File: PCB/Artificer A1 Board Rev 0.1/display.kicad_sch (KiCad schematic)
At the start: 24 parts

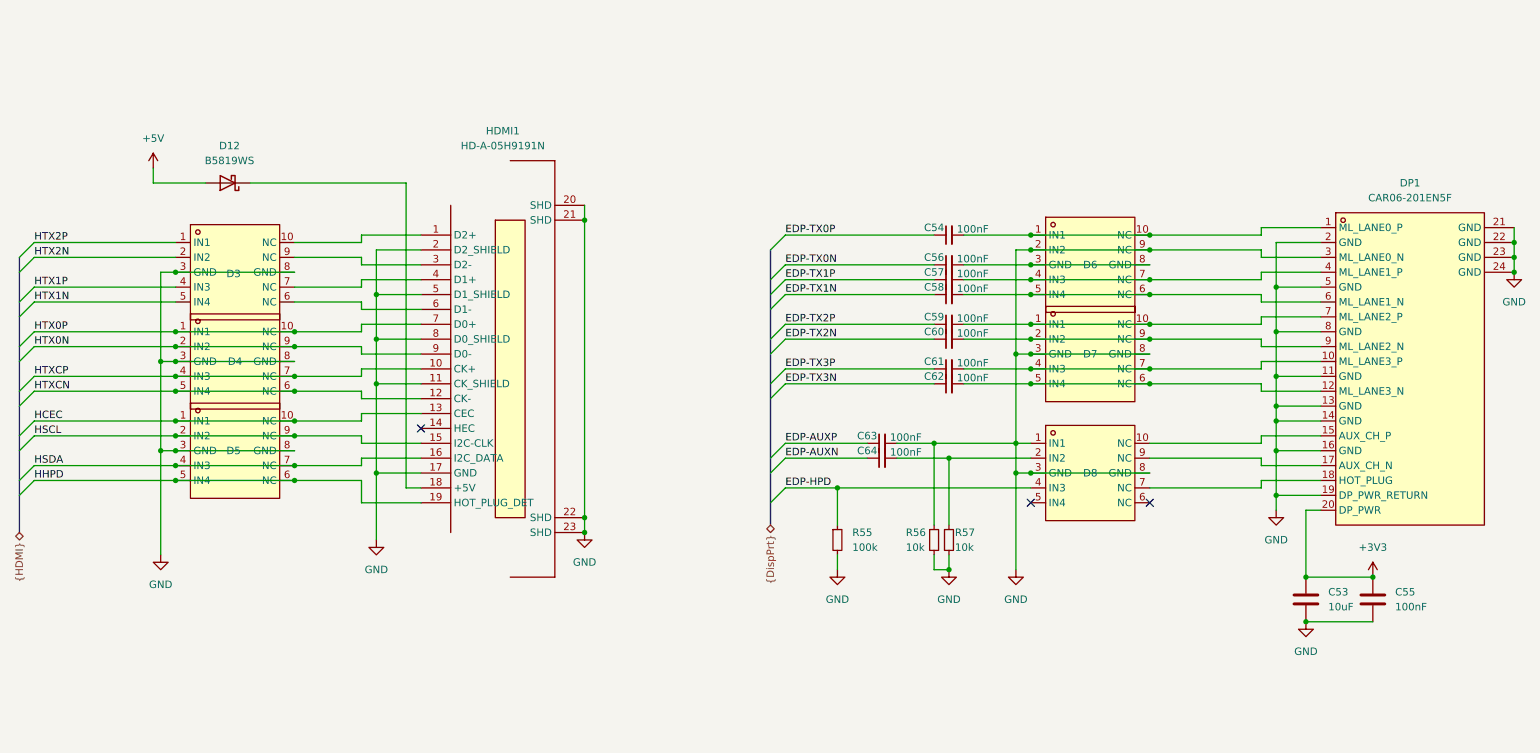
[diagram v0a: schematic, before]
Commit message: cleaned up, kicad 10 & usb c pd
migrated to Kicad 10,
added USB PD for power input
added capacitors inductors and resistor footprints
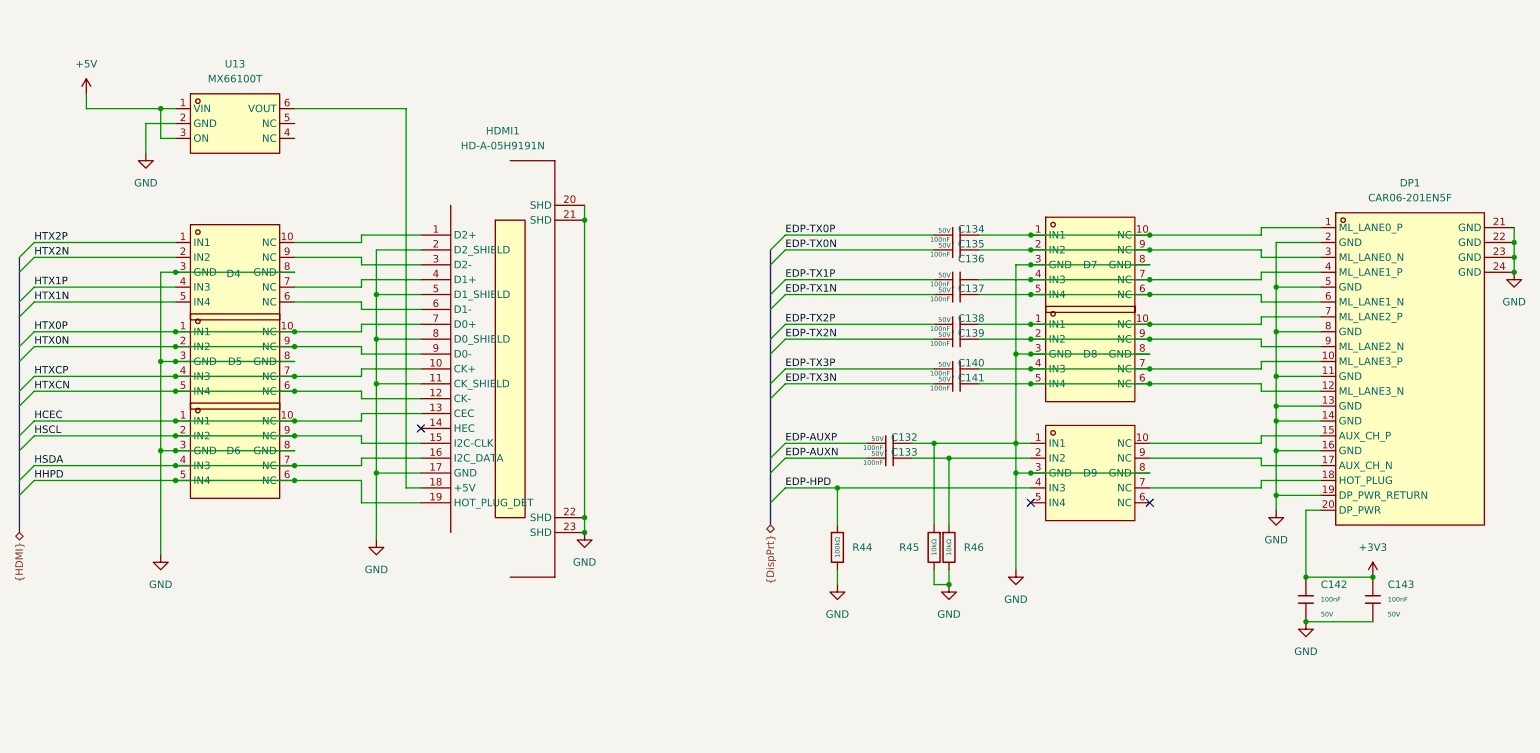
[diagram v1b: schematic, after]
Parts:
- removed C53: 10uF, symbol Device:C
- removed C54, C56, C57, C58, C59, C60, C61, C62, C63, C64: 100nF, symbol Device:C_Small
- removed C55: 100nF, symbol Device:C
- removed D12: B5819WS, Diode_SMD:D_SOD-323_HandSoldering, symbol Device:D_Schottky
- removed R55: 100k, symbol Device:R_Small
- removed R56, R57: 10k, symbol Device:R_Small
- added C132, C133, C134, C135, C136, C137, C138, C139, C140, C141, C142, C143: 100nF, PCM_JLCPCB:C_0402, symbol PCM_JLCPCB-Capacitors:0402,100nF,(2)
- added R44: 100kΩ, PCM_JLCPCB:R_0402, symbol PCM_JLCPCB-Resistors:0402,100kΩ
- added R45, R46: 10kΩ, PCM_JLCPCB:R_0402, symbol PCM_JLCPCB-Resistors:0402,10kΩ
- added U13: MX66100T, easyeda:SOT-23-6_L2.9-W1.6-P0.95-LS2.9-BL, symbol easyeda:MX66100T
- renumbered D3 to D4, D4 to D5, D5 to D6, D6 to D7, D7 to D8, D8 to D9
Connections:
- net +3V3: now also C142.1, C143.1
- net +5V: now also U13.1 (VIN), U13.3 (ON)
- net EDP-AUXN: now also C133.1
- net EDP-AUXP: now also C132.1
- net EDP-HPD: now also R44.1
- net EDP-TX0N: now also C135.1
- net EDP-TX0P: now also C134.1
- net EDP-TX1N: now also C137.1
- net EDP-TX1P: now also C136.1
- net EDP-TX2N: now also C139.1
- net EDP-TX2P: now also C138.1
- net EDP-TX3N: now also C141.1
- net EDP-TX3P: now also C140.1
- net GND: now also D7.3 (GND), D7.8 (GND), C132.2, C142.2, C143.2, R44.2, R45.1, R45.2, R46.2, U13.2 (GND); no longer D7.2 (IN2), D7.9 (NC), DP1.3 (ML_LANE0_N)
- net at D8.1 (IN1), D8.10 (NC), DP1.7 (ML_LANE2_P): now also C138.2
- net at D8.2 (IN2), D8.9 (NC), DP1.9 (ML_LANE2_N): now also C139.2
- net at D8.4 (IN3), D8.7 (NC), DP1.10 (ML_LANE3_P): now also C140.2
- net at D8.5 (IN4), D8.6 (NC), DP1.12 (ML_LANE3_N): now also C141.2
- net at D7.5 (IN4), D7.6 (NC), DP1.6 (ML_LANE1_N): now also C137.2
- net at D9.2 (IN2): now also C133.2, R46.1
- net at D7.4 (IN3), D7.7 (NC), DP1.4 (ML_LANE1_P): now also C136.2
- net at HDMI1.18 (+5V): now also U13.6 (VOUT)
- net at D7.1 (IN1), D7.10 (NC), DP1.1 (ML_LANE0_P): now also C134.2
- new net: C135.2, D7.2 (IN2), D7.9 (NC), DP1.3 (ML_LANE0_N)

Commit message: placed all components
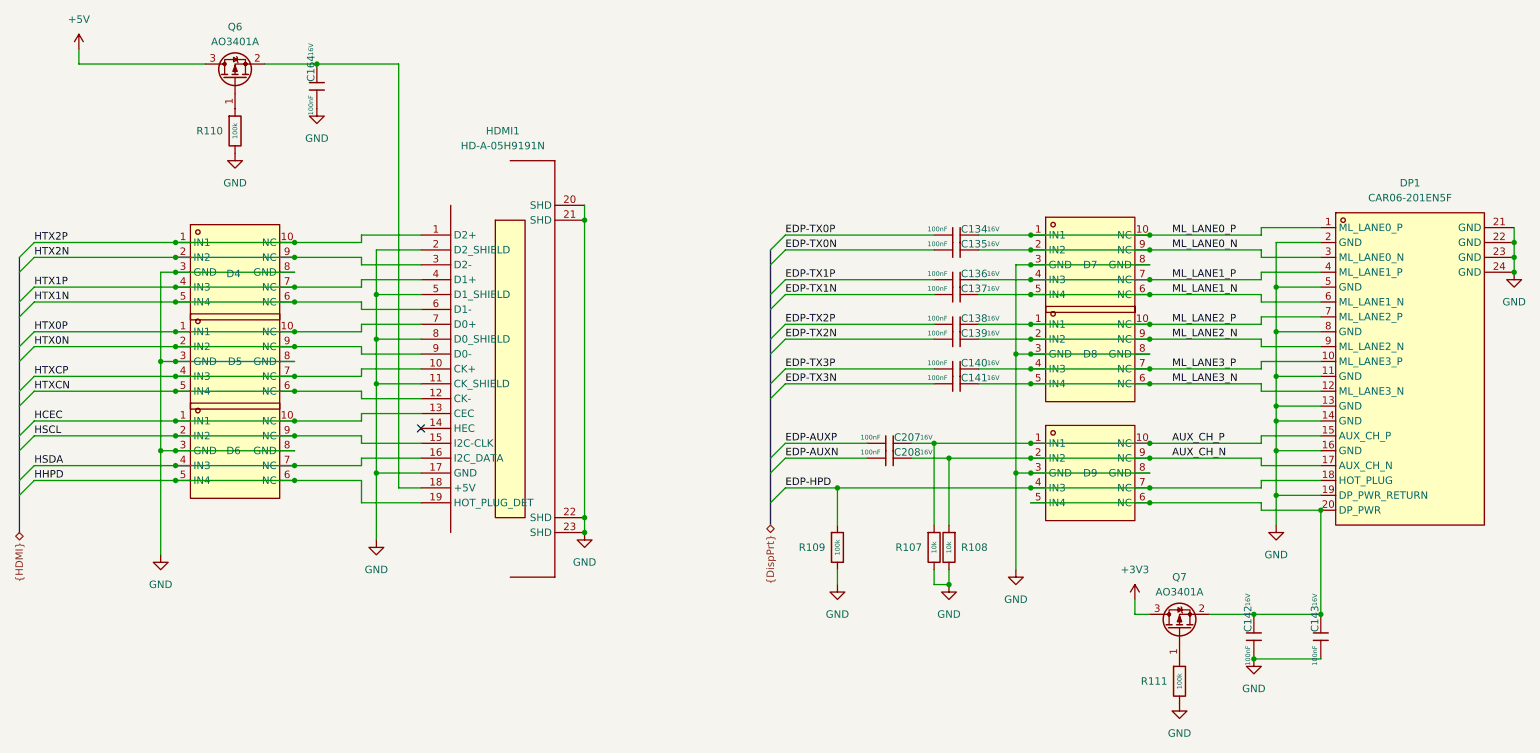
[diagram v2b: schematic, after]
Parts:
- removed C132, C133, C134, C135, C136, C137, C138, C139, C140, C141, C142, C143: 100nF, PCM_JLCPCB:C_0402, symbol PCM_JLCPCB-Capacitors:0402,100nF,(2)
- removed R44: 100kΩ, PCM_JLCPCB:R_0402, symbol PCM_JLCPCB-Resistors:0402,100kΩ
- removed R45, R46: 10kΩ, PCM_JLCPCB:R_0402, symbol PCM_JLCPCB-Resistors:0402,10kΩ
- removed U13: MX66100T, easyeda:SOT-23-6_L2.9-W1.6-P0.95-LS2.9-BL, symbol easyeda:MX66100T
- added C134, C135, C136, C137, C138, C139, C140, C141, C142, C143, C164, C207, C208: 100nF, Capacitor_SMD:C_0201_0603Metric, symbol Cap:JLCPCB_Lib_Blank_Cap
- added Q6, Q7: AO3401A, Package_TO_SOT_SMD:SOT-23, symbol Transistor_FET:AO3401A
- added R107, R108: 10k, Resistor_SMD:R_0201_0603Metric, symbol Cap:JLCPCB_Res_Custom
- added R109, R110, R111: 100k, Resistor_SMD:R_0201_0603Metric, symbol Cap:JLCPCB_Res_Custom
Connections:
- net +3V3: now also Q7.3 (D); no longer DP1.20 (DP_PWR)
- net +5V: now also Q6.3 (D)
- net EDP-AUXN: now also C208.1
- net EDP-AUXP: now also C207.1
- net EDP-HPD: now also D9.7 (NC), DP1.18 (HOT_PLUG), R109.1
- net EDP-TX0N: now also C135.1
- net EDP-TX0P: now also C134.1
- net EDP-TX1N: now also C137.1
- net EDP-TX1P: now also C136.1
- net EDP-TX2N: now also C139.1
- net EDP-TX2P: now also C138.1
- net EDP-TX3N: now also C141.1
- net EDP-TX3P: now also C140.1
- net GND: now also C142.1, C143.1, C164.1, R107.2, R108.2, R109.2, R110.2, R111.2; no longer D9.1 (IN1)
- net HTX1N: now also D4.6 (NC), HDMI1.6 (D1-)
- net HTX1P: now also D4.7 (NC), HDMI1.4 (D1+)
- net HTX2N: now also D4.9 (NC), HDMI1.3 (D2-)
- net HTX2P: now also D4.10 (NC), HDMI1.1 (D2+)
- net AUX_CH_N: now reaches D9.2 (IN2)
- net AUX_CH_N: now also D9.9 (NC), DP1.17 (AUX_CH_N), C208.2, R108.1
- net ML_LANE2_P: now reaches D8.1 (IN1), D8.10 (NC), DP1.7 (ML_LANE2_P)
- net ML_LANE2_P: now also C138.2
- net ML_LANE2_N: now reaches D8.2 (IN2), D8.9 (NC), DP1.9 (ML_LANE2_N)
- net ML_LANE2_N: now also C139.2
- net ML_LANE3_P: now reaches D8.4 (IN3), D8.7 (NC), DP1.10 (ML_LANE3_P)
- net ML_LANE3_P: now also C140.2
- net ML_LANE3_N: now reaches D8.5 (IN4), D8.6 (NC), DP1.12 (ML_LANE3_N)
- net ML_LANE3_N: now also C141.2
- net at HDMI1.18 (+5V): now also C164.2, Q6.2 (S)
- net ML_LANE0_P: now reaches D7.1 (IN1), D7.10 (NC), DP1.1 (ML_LANE0_P)
- net ML_LANE0_P: now also C134.2
- net AUX_CH_P: now reaches D9.10 (NC), DP1.15 (AUX_CH_P)
- net AUX_CH_P: now also D9.1 (IN1), C207.2, R107.1
- net at D9.5 (IN4): now also D9.6 (NC), DP1.20 (DP_PWR), C142.2, C143.2, Q7.2 (S)
- net ML_LANE1_N: now reaches D7.5 (IN4), D7.6 (NC), DP1.6 (ML_LANE1_N)
- net ML_LANE1_N: now also C137.2
- net ML_LANE0_N: now reaches D7.2 (IN2), D7.9 (NC), DP1.3 (ML_LANE0_N)
- net ML_LANE0_N: now also C135.2
- net ML_LANE1_P: now reaches D7.4 (IN3), D7.7 (NC), DP1.4 (ML_LANE1_P)
- net ML_LANE1_P: now also C136.2
- new net: Q7.1 (G), R111.1
- new net: Q6.1 (G), R110.1
- no-connect marks 3 -> 1

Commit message: worked on power pours
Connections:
- net +3V3 renamed VCC-3V3
- net +5V renamed 5V_SYS
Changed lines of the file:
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@@
+	)
+	(symbol
+		(lib_id "power:+5V")
+		(at 27.94 43.18 0)
+		(unit 1)
+		(body_style 1)
+		(exclude_from_sim no)
+		(in_bom yes)
+		(on_board yes)
+		(in_pos_files yes)
+		(dnp no)
+		(property "Reference" "#PWR0264"
+			(at 27.94 46.99 0)
+			(hide yes)
+			(show_name no)
+			(do_not_autoplace no)
+			(effects
+				(font
+					(size 1.27 1.27)
+				)
+			)
+		)
+		(property "Value" "5V_SYS"
+			(at 32.766 41.656 0)
+			(show_name no)
+			(do_not_autoplace no)
+			(effects
+				(font
+					(size 1.27 1.27)
+				)
+			)
+		)
+		(property "Footprint" ""
+			(at 27.94 43.18 0)
+			(hide yes)
+			(show_name no)
+			(do_not_autoplace no)
+			(effects
+				(font
+					(size 1.27 1.27)
+				)
+			)
+		)
+		(property "Datasheet" ""
+			(at 27.94 43.18 0)
+			(hide yes)
+			(show_name no)
+			(do_not_autoplace no)
+			(effects
+				(font
+					(size 1.27 1.27)
+				)
+			)
+		)
+		(property "Description" "Power symbol creates a global label with name \"+5V\""
+			(at 27.94 43.18 0)
+			(hide yes)
+			(show_name no)
+			(do_not_autoplace no)
+			(effects
+				(font
+					(size 1.27 1.27)
+				)
+			)
+		)
+		(pin "1"
+		)
+		(instances
+			(project "Artificer A1 Board Rev 0.1"
+				(path "/7c37bdb5-94b0-4567-b5ec-a879db855389/0eff4a68-7f18-47e2-a88b-bcc4ad7e7e86"
+					(reference "#PWR0264")
+					(unit 1)
+				)
+			)
+		)
 	)
 	(symbol
@@
 	)
 	(symbol
-		(lib_id "power:+5V")
-		(at 27.94 43.18 0)
-		(unit 1)
-		(body_style 1)
-		(exclude_from_sim no)
-		(in_bom yes)
-		(on_board yes)
-		(in_pos_files yes)
-		(dnp no)
-		(fields_autoplaced yes)
-		(property "Reference" "#PWR0264"
-			(at 27.94 46.99 0)
-			(hide yes)
-			(show_name no)
-			(do_not_autoplace no)
-			(effects
-				(font
-					(size 1.27 1.27)
-				)
-			)
-		)
-		(property "Value" "+5V"
-			(at 27.94 38.1 0)
-			(show_name no)
-			(do_not_autoplace no)
-			(effects
-				(font
-					(size 1.27 1.27)
-				)
-			)
-		)
-		(property "Footprint" ""
-			(at 27.94 43.18 0)
-			(hide yes)
-			(show_name no)
-			(do_not_autoplace no)
-			(effects
-				(font
-					(size 1.27 1.27)
-				)
-			)
-		)
-		(property "Datasheet" ""
-			(at 27.94 43.18 0)
-			(hide yes)
-			(show_name no)
-			(do_not_autoplace no)
-			(effects
-				(font
-					(size 1.27 1.27)
-				)
-			)
-		)
-		(property "Description" "Power symbol creates a global label with name \"+5V\""
-			(at 27.94 43.18 0)
-			(hide yes)
-			(show_name no)
-			(do_not_autoplace no)
-			(effects
-				(font
-					(size 1.27 1.27)
-				)
-			)
-		)
-		(pin "1"
-		)
-		(instances
-			(project "Artificer A1 Board Rev 0.1"
-				(path "/7c37bdb5-94b0-4567-b5ec-a879db855389/0eff4a68-7f18-47e2-a88b-bcc4ad7e7e86"
-					(reference "#PWR0264")
-					(unit 1)
-				)
-			)
-		)
-	)
-	(symbol
 		(lib_id "Cap:JLCPCB_Lib_Blank_Cap")
 		(at 228.6 143.51 180)
@@
 				(path "/7c37bdb5-94b0-4567-b5ec-a879db855389/0eff4a68-7f18-47e2-a88b-bcc4ad7e7e86"
 					(reference "C142")
-					(unit 1)
-				)
-			)
-		)
-	)
-	(symbol
-		(lib_id "power:+3V3")
-		(at 208.28 137.16 0)
-		(unit 1)
-		(body_style 1)
-		(exclude_from_sim no)
-		(in_bom yes)
-		(on_board yes)
-		(in_pos_files yes)
-		(dnp no)
-		(fields_autoplaced yes)
-		(property "Reference" "#PWR0274"
-			(at 208.28 140.97 0)
-			(hide yes)
-			(show_name no)
-			(do_not_autoplace no)
-			(effects
-				(font
-					(size 1.27 1.27)
-				)
-			)
-		)
-		(property "Value" "+3V3"
-			(at 208.28 132.08 0)
-			(show_name no)
-			(do_not_autoplace no)
-			(effects
-				(font
-					(size 1.27 1.27)
-				)
-			)
-		)
-		(property "Footprint" ""
-			(at 208.28 137.16 0)
-			(hide yes)
-			(show_name no)
-			(do_not_autoplace no)
-			(effects
-				(font
-					(size 1.27 1.27)
-				)
-			)
-		)
-		(property "Datasheet" ""
-			(at 208.28 137.16 0)
-			(hide yes)
-			(show_name no)
-			(do_not_autoplace no)
-			(effects
-				(font
-					(size 1.27 1.27)
-				)
-			)
-		)
-		(property "Description" "Power symbol creates a global label with name \"+3V3\""
-			(at 208.28 137.16 0)
-			(hide yes)
-			(show_name no)
-			(do_not_autoplace no)
-			(effects
-				(font
-					(size 1.27 1.27)
-				)
-			)
-		)
-		(pin "1"
-		)
-		(instances
-			(project "Artificer A1 Board Rev 0.1"
-				(path "/7c37bdb5-94b0-4567-b5ec-a879db855389/0eff4a68-7f18-47e2-a88b-bcc4ad7e7e86"
-					(reference "#PWR0274")
 					(unit 1)
 				)
@@
 					(unit 1)
 				)
+			)
+		)
+	)
+	(symbol
+		(lib_id "power:+5V")
+		(at 208.28 137.16 0)
+		(unit 1)
+		(body_style 1)
+		(exclude_from_sim no)
+		(in_bom yes)
+		(on_board yes)
+		(in_pos_files yes)
+		(dnp no)
+		(property "Reference" "#PWR0274"
+			(at 208.28 140.97 0)
+			(hide yes)
+			(show_name no)
+			(do_not_autoplace no)
+			(effects
+				(font
+					(size 1.27 1.27)
+				)
+			)
+		)
+		(property "Value" "VCC-3V3"
+			(at 200.406 135.636 0)
+			(show_name no)
+			(do_not_autoplace no)
+			(effects
+				(font
+					(size 1.27 1.27)
+				)
+			)
+		)
+		(property "Footprint" ""
+			(at 208.28 137.16 0)
+			(hide yes)
+			(show_name no)
+			(do_not_autoplace no)
+			(effects
+				(font
+					(size 1.27 1.27)
+				)
+			)
+		)
+		(property "Datasheet" ""
+			(at 208.28 137.16 0)
+			(hide yes)
+			(show_name no)
+			(do_not_autoplace no)
+			(effects
+				(font
+					(size 1.27 1.27)
+				)
+			)
+		)
+		(property "Description" "Power symbol creates a global label with name \"+5V\""
+			(at 208.28 137.16 0)
+			(hide yes)
+			(show_name no)
+			(do_not_autoplace no)
+			(effects
+				(font
+					(size 1.27 1.27)
+				)
+			)
+		)
+		(pin "1"
+		)
+		(instances
+			(project "Artificer A1 Board Rev 0.1"
+				(path "/7c37bdb5-94b0-4567-b5ec-a879db855389/0eff4a68-7f18-47e2-a88b-bcc4ad7e7e86"
+					(reference "#PWR0274")
+					(unit 1)
+				)
